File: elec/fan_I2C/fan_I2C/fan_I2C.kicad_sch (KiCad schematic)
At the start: 16 parts, among them J101 DB25_Female_MountingHoles, J102 DB9_Female_MountingHoles, SW101 SW_DIP_x08

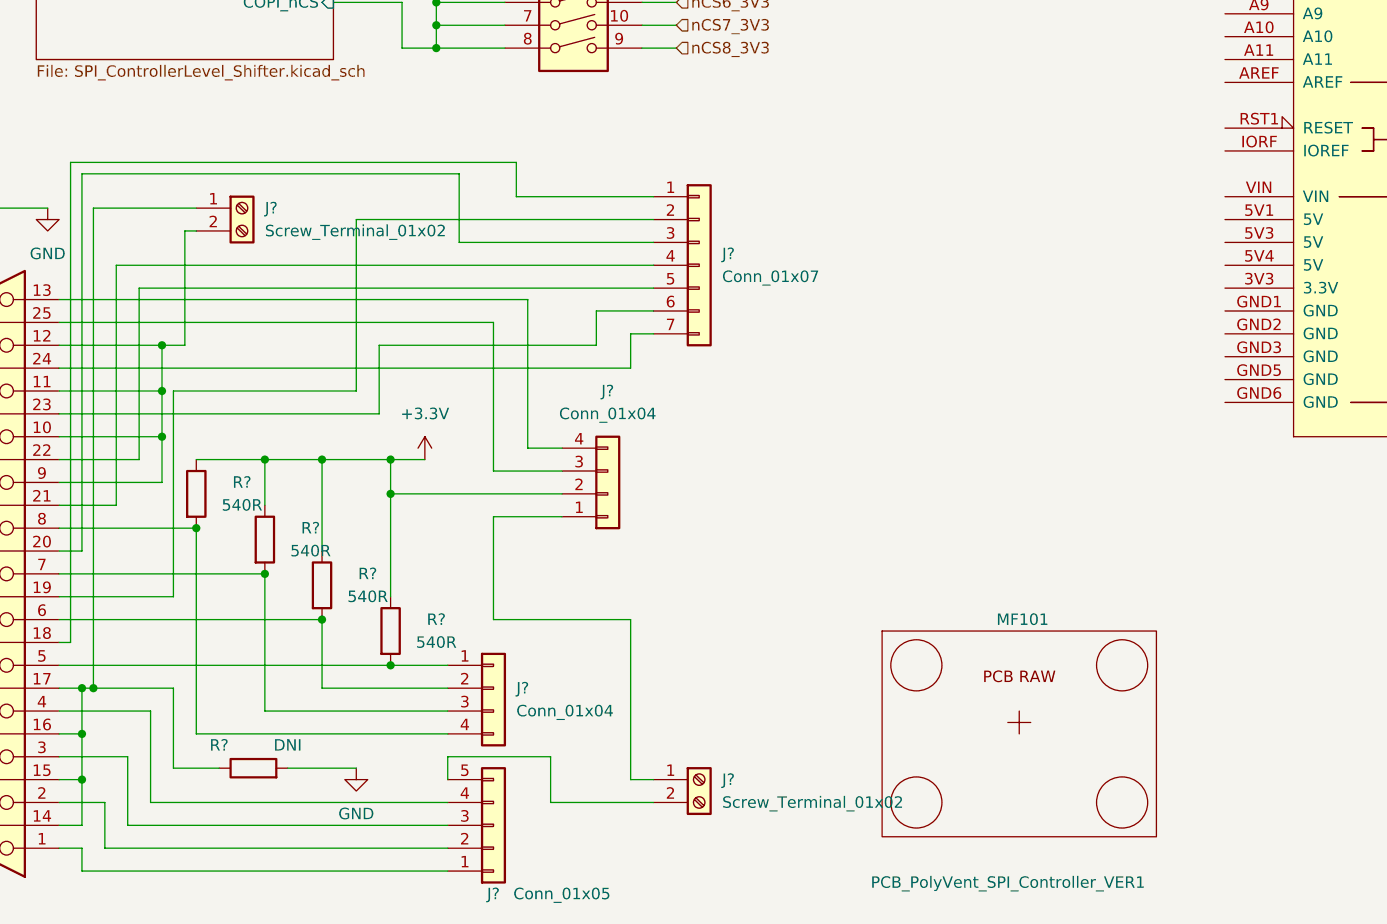
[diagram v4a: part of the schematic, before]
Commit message: Add connect Due 3V3, 5V and gnd.
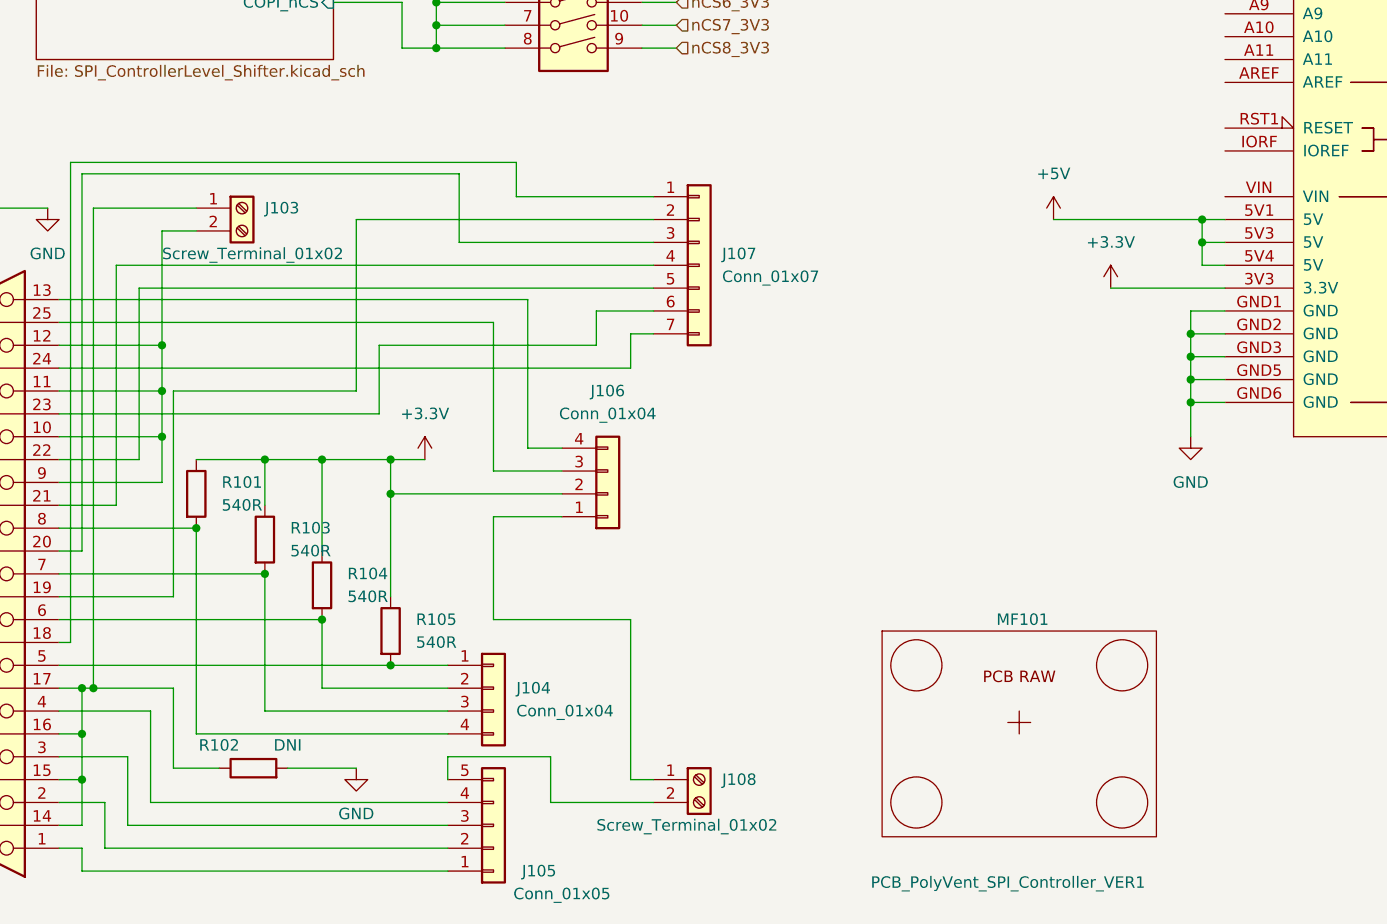
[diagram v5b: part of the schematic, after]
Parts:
- J103, J108: renamed from J?; footprint (none) -> TerminalBlock_MetzConnect:TerminalBlock_MetzConnect_Type073_RT02602HBLU_1x02_P5.08mm_Horizontal
- gave numbers to parts that had none: 9
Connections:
- net +3.3V: now also XA101.3V3 (3.3V)
- net +5V: now also XA101.5V1 (5V), XA101.5V3 (5V), XA101.5V4 (5V)
- net GND: now also XA101.GND1 (GND), XA101.GND2 (GND), XA101.GND3 (GND), XA101.GND5 (GND), XA101.GND6 (GND)

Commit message: Tweeks, perhaps some schematic notes.
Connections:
- net GND: now also J106.1 (Pin_1), J108.1 (Pin_1)
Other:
- note added: "+12V"
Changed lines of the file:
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@@
   (junction (at 73.66 100.33) (diameter 0) (color 0 0 0 0)
   )
+  (junction (at 80.01 166.37) (diameter 0) (color 0 0 0 0)
+  )
   (junction (at 34.29 179.07) (diameter 0) (color 0 0 0 0)
   )
@@
     (stroke (width 0) (type default) (color 0 0 0 0))
   )
+  (wire (pts (xy 80.01 166.37) (xy 80.01 160.02))
+    (stroke (width 0) (type default) (color 0 0 0 0))
+  )
   (wire (pts (xy 96.52 97.79) (xy 100.33 97.79))
     (stroke (width 0) (type default) (color 0 0 0 0))
@@
     (stroke (width 0) (type default) (color 0 0 0 0))
   )
+  (wire (pts (xy 80.01 166.37) (xy 99.06 166.37))
+    (stroke (width 0) (type default) (color 0 0 0 0))
+  )
   (wire (pts (xy 44.45 179.07) (xy 44.45 187.96))
     (stroke (width 0) (type default) (color 0 0 0 0))
@@
     (stroke (width 0) (type default) (color 0 0 0 0))
   )
-  (wire (pts (xy 80.01 171.45) (xy 80.01 160.02))
+  (wire (pts (xy 80.01 171.45) (xy 80.01 166.37))
     (stroke (width 0) (type default) (color 0 0 0 0))
   )
@@
     )
   )
+  (text "+12V" (at 54.61 129.54 0)
+    (effects (font (size 1.27 1.27)) (justify left bottom))
+  )
   (global_label "COPI" (shape input) (at 76.2 77.47 0) (fields_autoplaced)
     (effects (font (size 1.27 1.27)) (justify left))
@@
     )
   )
+  (symbol (lib_id "power:GND") (at 99.06 166.37 0) (unit 1)
+    (in_bom yes) (on_board yes) (fields_autoplaced)
+    (property "Reference" "#PWR?" (id 0) (at 99.06 172.72 0)
+      (effects (font (size 1.27 1.27)) hide)
+    )
+    (property "Value" "GND" (id 1) (at 99.06 171.45 0))
+    (property "Footprint" "" (id 2) (at 99.06 166.37 0)
+      (effects (font (size 1.27 1.27)) hide)
+    )
+    (property "Datasheet" "" (id 3) (at 99.06 166.37 0)
+      (effects (font (size 1.27 1.27)) hide)
+    )
+    (pin "1")
+  )
   (symbol (lib_id "Connector:DB9_Female_MountingHoles") (at 25.4 48.26 180) (unit 1)
     (in_bom yes) (on_board yes) (fields_autoplaced)
@@
       (reference "#PWR?") (unit 1) (value "+3.3V") (footprint "")
     )
+    (path "/c82c20b0-3df2-4b88-9f84-d1ea37c18e52"
+      (reference "#PWR?") (unit 1) (value "GND") (footprint "")
+    )
     (path "/09141fd0-c295-4cc6-88a0-924ace0abc49/41603e1f-8af5-450c-b894-83c4b3ed5006"

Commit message: Add text notes????
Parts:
- added J109: Conn_02x12_Odd_Even, Connector_JST:JST_PHD_B24B-PHDSS_2x12_P2.00mm_Vertical, symbol Connector_Generic:Conn_02x12_Odd_Even
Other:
- note added: "| **Pin #** | **Function** | **Description** | **Pin #** | **Function** | **Description** | |----------- |-------------- |-------------------------------------- |----------- |-------------- |-------------------------------------- | | 1 | VS+ | Remote Sense (+) | 13 | ACI | I Program | | 2 | VO+ | Positive Output Voltage | 14 | GND | Ground | | 3 | VX- | Remote Sense (-) | 15 | VCI | V Program | |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"

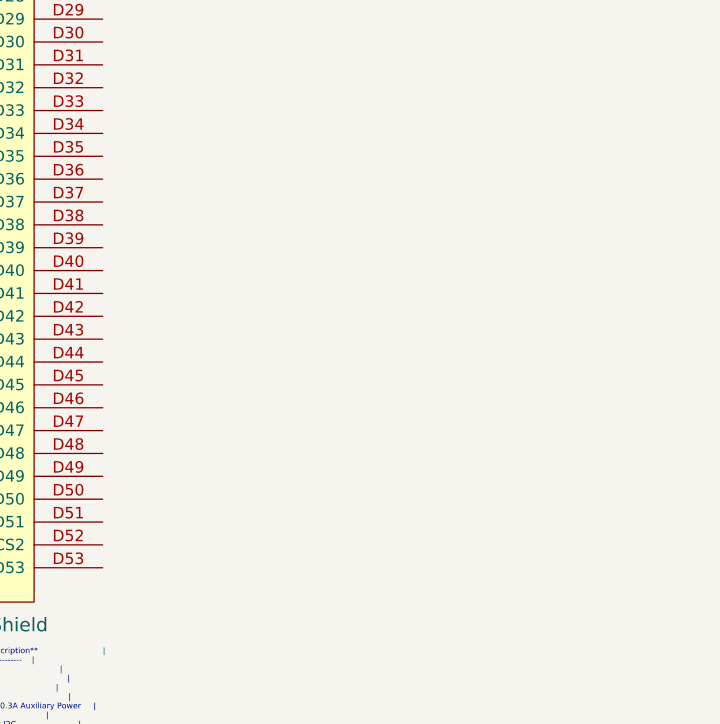
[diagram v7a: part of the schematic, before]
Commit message: Add mounting holes.
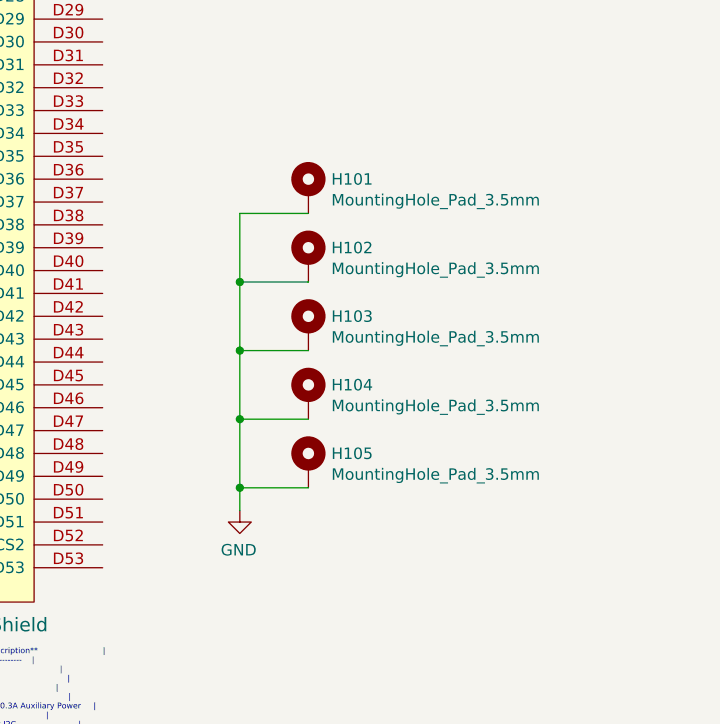
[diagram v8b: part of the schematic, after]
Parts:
- added H101, H102, H103, H104, H105: MountingHole_Pad_3.5mm, GeneralPurposeAlarmDevicePCB:MountingHole_3.5mm_Pad_Via, symbol GPAD_SCH_LIB:MountingHole_Pad_3.5mm
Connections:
- net GND: now also H101.1, H102.1, H103.1, H104.1, H105.1
